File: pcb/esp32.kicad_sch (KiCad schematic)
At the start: 14 parts, among them J1 USB_C_Receptacle_USB2.0_16P, U1 ESP32-S3-WROOM-1, U2 AP2112K-3.3

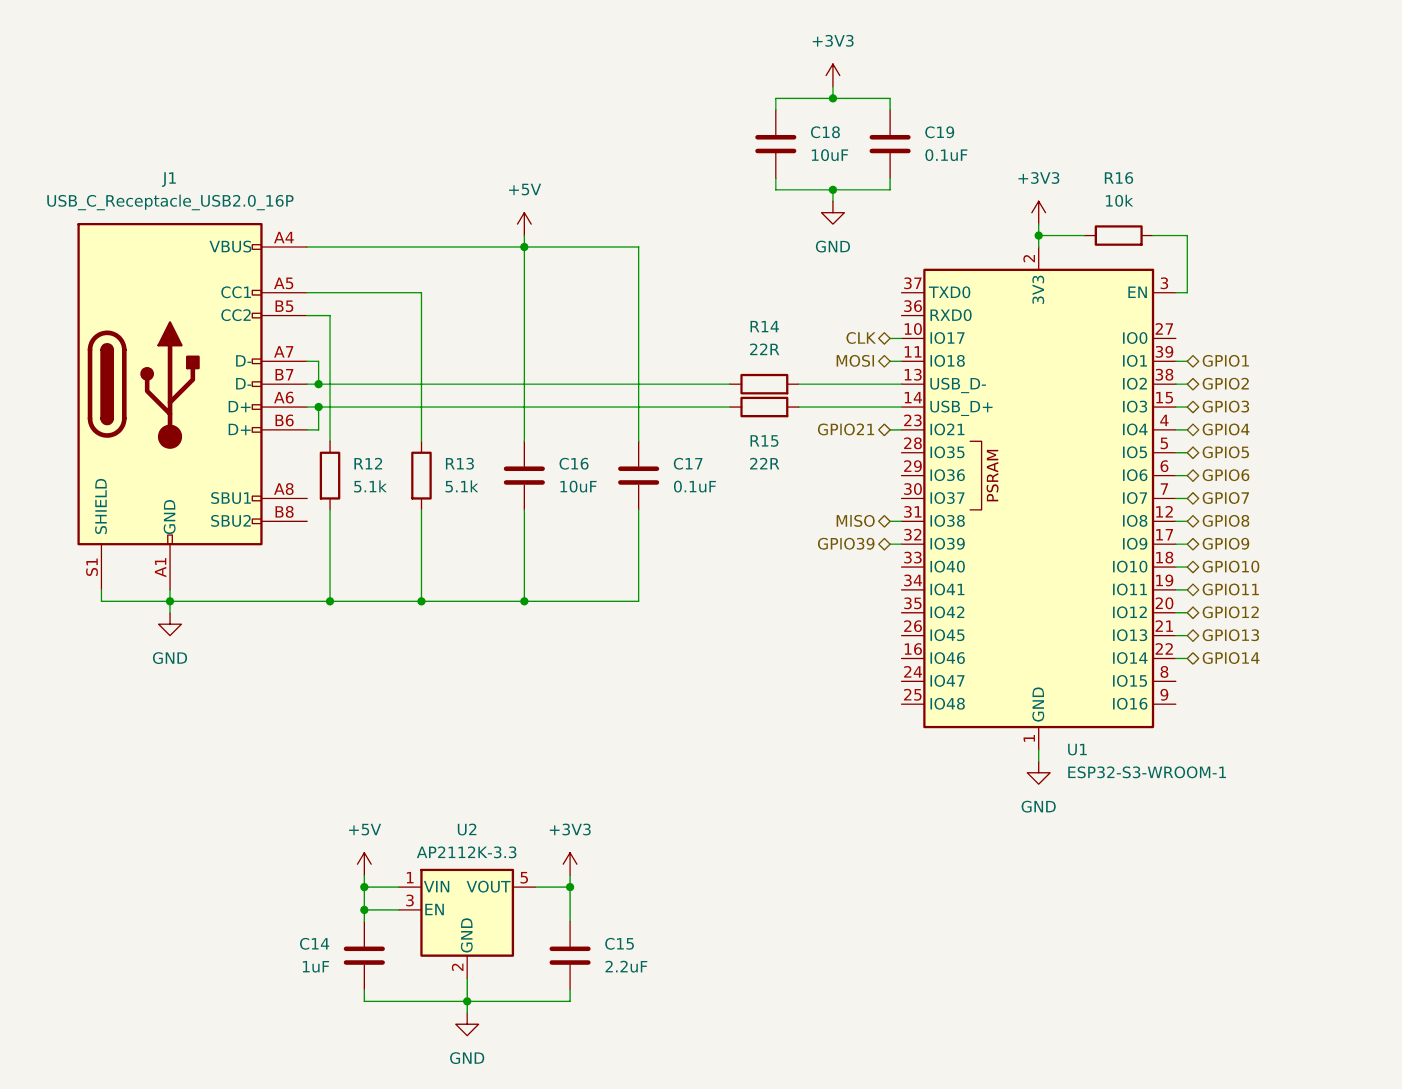
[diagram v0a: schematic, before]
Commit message: Fixed 3.3V connections and SD card orientation
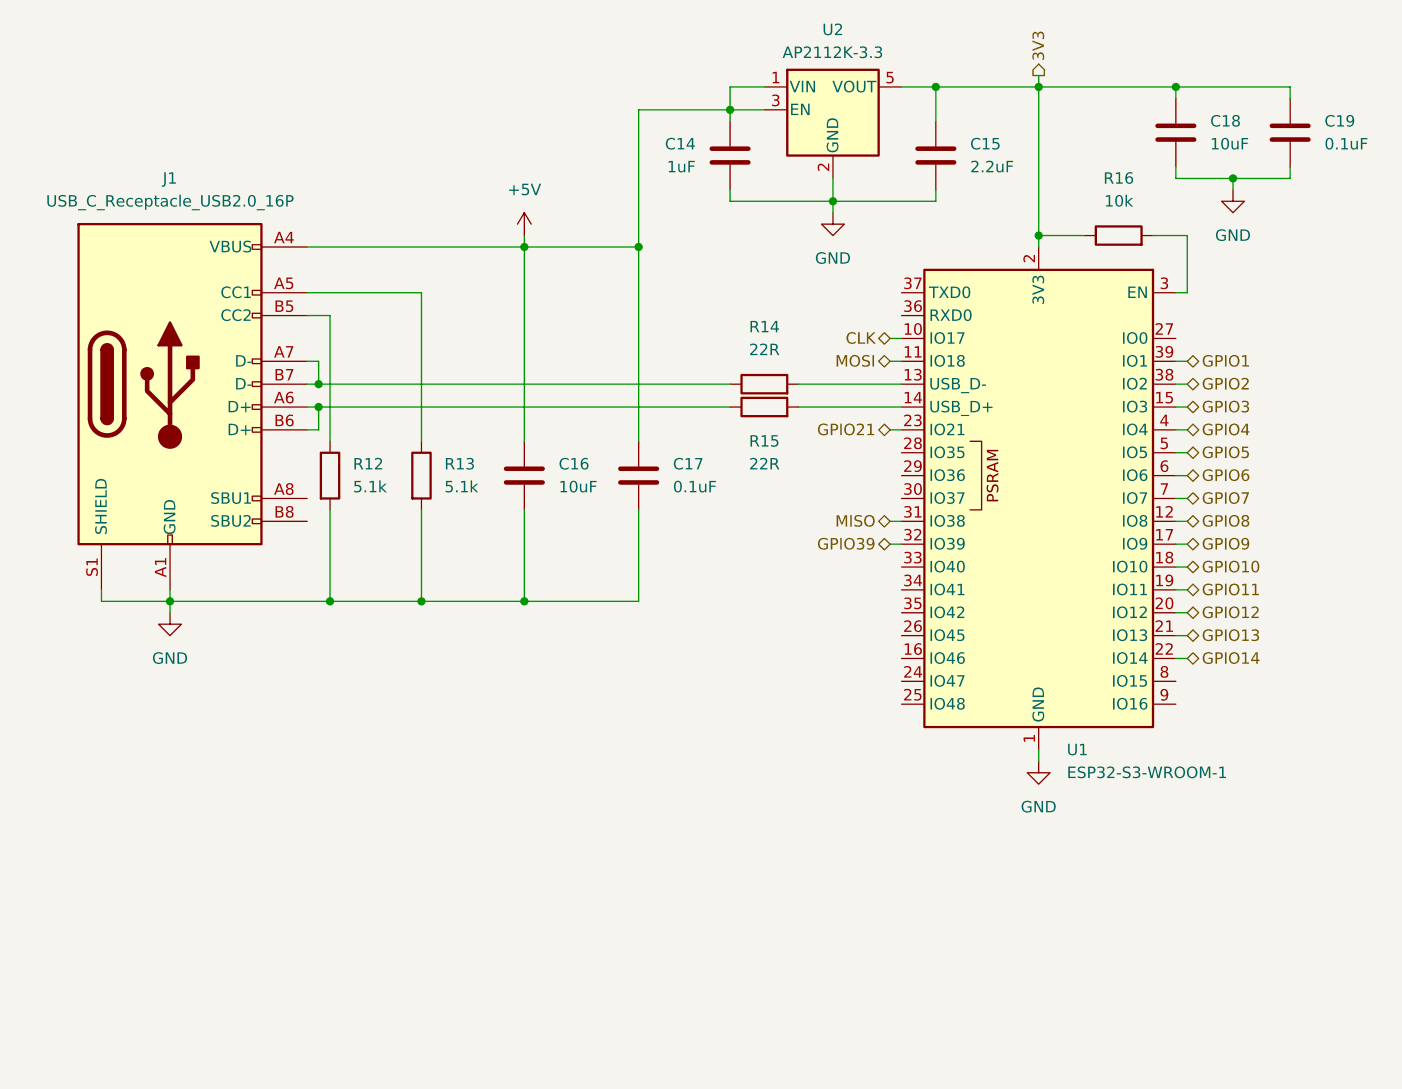
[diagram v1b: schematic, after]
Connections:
- net +3V3 renamed 3V3
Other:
- moved on the sheet: C14, C15, C18, C19, U2

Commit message: Added SSD1327 circuit
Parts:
- renumbered C16 to C1, C17 to C2, C14 to C3, C15 to C4, C18 to C5, C19 to C6, J1 to J2, U2 to U1, U1 to U2

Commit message: Split PCB into modules
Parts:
- renumbered C1 to C4, C2 to C5, C3 to C6, C4 to C7, C5 to C8, C6 to C9, J2 to J3, R12 to R4, R13 to R5, R14 to R6, R15 to R7, R16 to R8

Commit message: SSD1327 PCB routing
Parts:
- renumbered C4 to C3, C5 to C4, C6 to C5, C7 to C6, C8 to C7, C9 to C8, R4 to R3, R5 to R4, R6 to R5, R7 to R6, R8 to R7
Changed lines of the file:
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@@
 		(dnp no)
 		(fields_autoplaced yes)
-		(property "Reference" "R8"
+		(property "Reference" "R7"
 			(at 187.96 44.45 90)
 			(effects
@@
 		)
 		(instances
+			(project "ssd1327"
+				(path "/4342a6a3-bef3-4d00-bf81-0e0627ac4f3c/89317fe1-37c2-417c-ae91-da35df10ccc3"
+					(reference "R7")
+					(unit 1)
+				)
+			)
 			(project "ssd1322"
 				(path "/e965cf35-0f43-4e18-a922-fe79a625b049/6582fc17-a6be-4359-8e04-c0b6227802a5"
@@
 		(dnp no)
 		(fields_autoplaced yes)
-		(property "Reference" "R4"
+		(property "Reference" "R3"
 			(at 102.87 76.1999 0)
 			(effects
@@
 		)
 		(instances
+			(project "ssd1327"
+				(path "/4342a6a3-bef3-4d00-bf81-0e0627ac4f3c/89317fe1-37c2-417c-ae91-da35df10ccc3"
+					(reference "R3")
+					(unit 1)
+				)
+			)
 			(project "ssd1322"
 				(path "/e965cf35-0f43-4e18-a922-fe79a625b049/6582fc17-a6be-4359-8e04-c0b6227802a5"
@@
 		(dnp no)
 		(fields_autoplaced yes)
-		(property "Reference" "C4"
+		(property "Reference" "C3"
 			(at 125.73 76.1999 0)
 			(effects
@@
 		)
 		(instances
+			(project "ssd1327"
+				(path "/4342a6a3-bef3-4d00-bf81-0e0627ac4f3c/89317fe1-37c2-417c-ae91-da35df10ccc3"
+					(reference "C3")
+					(unit 1)
+				)
+			)
 			(project "ssd1322"
 				(path "/e965cf35-0f43-4e18-a922-fe79a625b049/6582fc17-a6be-4359-8e04-c0b6227802a5"
@@
 		)
 		(instances
+			(project "ssd1327"
+				(path "/4342a6a3-bef3-4d00-bf81-0e0627ac4f3c/89317fe1-37c2-417c-ae91-da35df10ccc3"
+					(reference "J3")
+					(unit 1)
+				)
+			)
 			(project "ssd1322"
 				(path "/e965cf35-0f43-4e18-a922-fe79a625b049/6582fc17-a6be-4359-8e04-c0b6227802a5"
@@
 		(dnp no)
 		(fields_autoplaced yes)
-		(property "Reference" "C8"
+		(property "Reference" "C7"
 			(at 198.12 38.0999 0)
 			(effects
@@
 		)
 		(instances
+			(project "ssd1327"
+				(path "/4342a6a3-bef3-4d00-bf81-0e0627ac4f3c/89317fe1-37c2-417c-ae91-da35df10ccc3"
+					(reference "C7")
+					(unit 1)
+				)
+			)
 			(project "ssd1322"
 				(path "/e965cf35-0f43-4e18-a922-fe79a625b049/6582fc17-a6be-4359-8e04-c0b6227802a5"
@@
 		)
 		(instances
+			(project "ssd1327"
+				(path "/4342a6a3-bef3-4d00-bf81-0e0627ac4f3c/89317fe1-37c2-417c-ae91-da35df10ccc3"
+					(reference "#PWR08")
+					(unit 1)
+				)
+			)
 			(project "ssd1322"
 				(path "/e965cf35-0f43-4e18-a922-fe79a625b049/6582fc17-a6be-4359-8e04-c0b6227802a5"
@@
 		(dnp no)
 		(fields_autoplaced yes)
-		(property "Reference" "R5"
+		(property "Reference" "R4"
 			(at 113.03 76.1999 0)
 			(effects
@@
 		)
 		(instances
+			(project "ssd1327"
+				(path "/4342a6a3-bef3-4d00-bf81-0e0627ac4f3c/89317fe1-37c2-417c-ae91-da35df10ccc3"
+					(reference "R4")
+					(unit 1)
+				)
+			)
 			(project "ssd1322"
 				(path "/e965cf35-0f43-4e18-a922-fe79a625b049/6582fc17-a6be-4359-8e04-c0b6227802a5"
@@
 		)
 		(instances
+			(project "ssd1327"
+				(path "/4342a6a3-bef3-4d00-bf81-0e0627ac4f3c/89317fe1-37c2-417c-ae91-da35df10ccc3"
+					(reference "#PWR06")
+					(unit 1)
+				)
+			)
 			(project "ssd1322"
 				(path "/e965cf35-0f43-4e18-a922-fe79a625b049/6582fc17-a6be-4359-8e04-c0b6227802a5"
@@
 		(dnp no)
 		(fields_autoplaced yes)
-		(property "Reference" "C5"
+		(property "Reference" "C4"
 			(at 138.43 76.1999 0)
 			(effects
@@
 		)
 		(instances
+			(project "ssd1327"
+				(path "/4342a6a3-bef3-4d00-bf81-0e0627ac4f3c/89317fe1-37c2-417c-ae91-da35df10ccc3"
+					(reference "C4")
+					(unit 1)
+				)
+			)
 			(project "ssd1322"
 				(path "/e965cf35-0f43-4e18-a922-fe79a625b049/6582fc17-a6be-4359-8e04-c0b6227802a5"
@@
 		)
 		(instances
+			(project "ssd1327"
+				(path "/4342a6a3-bef3-4d00-bf81-0e0627ac4f3c/89317fe1-37c2-417c-ae91-da35df10ccc3"
+					(reference "U1")
+					(unit 1)
+				)
+			)
 			(project "ssd1322"
 				(path "/e965cf35-0f43-4e18-a922-fe79a625b049/6582fc17-a6be-4359-8e04-c0b6227802a5"
@@
 		(dnp no)
 		(fields_autoplaced yes)
-		(property "Reference" "R7"
+		(property "Reference" "R6"
 			(at 148.59 73.66 90)
 			(effects
@@
 		)
 		(instances
+			(project "ssd1327"
+				(path "/4342a6a3-bef3-4d00-bf81-0e0627ac4f3c/89317fe1-37c2-417c-ae91-da35df10ccc3"
+					(reference "R6")
+					(unit 1)
+				)
+			)
 			(project "ssd1322"
 				(path "/e965cf35-0f43-4e18-a922-fe79a625b049/6582fc17-a6be-4359-8e04-c0b6227802a5"
@@
 		(dnp no)
 		(fields_autoplaced yes)
-		(property "Reference" "R6"
+		(property "Reference" "R5"
 			(at 148.59 60.96 90)
 			(effects
@@
 		)
 		(instances
+			(project "ssd1327"
+				(path "/4342a6a3-bef3-4d00-bf81-0e0627ac4f3c/89317fe1-37c2-417c-ae91-da35df10ccc3"
+					(reference "R5")
+					(unit 1)
+				)
+			)
 			(project "ssd1322"
 				(path "/e965cf35-0f43-4e18-a922-fe79a625b049/6582fc17-a6be-4359-8e04-c0b6227802a5"
@@
 		)
 		(instances
+			(project "ssd1327"
+				(path "/4342a6a3-bef3-4d00-bf81-0e0627ac4f3c/89317fe1-37c2-417c-ae91-da35df10ccc3"
+					(reference "#PWR05")
+					(unit 1)
+				)
+			)
 			(project "ssd1322"
 				(path "/e965cf35-0f43-4e18-a922-fe79a625b049/6582fc17-a6be-4359-8e04-c0b6227802a5"
@@
 		)
 		(instances
+			(project "ssd1327"
+				(path "/4342a6a3-bef3-4d00-bf81-0e0627ac4f3c/89317fe1-37c2-417c-ae91-da35df10ccc3"
+					(reference "U2")
+					(unit 1)
+				)
+			)
 			(project "ssd1322"
 				(path "/e965cf35-0f43-4e18-a922-fe79a625b049/6582fc17-a6be-4359-8e04-c0b6227802a5"
@@
 		(dnp no)
 		(fields_autoplaced yes)
-		(property "Reference" "C6"
+		(property "Reference" "C5"
 			(at 140.97 40.6399 0)
 			(effects
@@
 		)
 		(instances
+			(project "ssd1327"
+				(path "/4342a6a3-bef3-4d00-bf81-0e0627ac4f3c/89317fe1-37c2-417c-ae91-da35df10ccc3"
+					(reference "C5")
+					(unit 1)
+				)
+			)
 			(project "ssd1322"
 				(path "/e965cf35-0f43-4e18-a922-fe79a625b049/6582fc17-a6be-4359-8e04-c0b6227802a5"
@@
 		)
 		(instances
+			(project "ssd1327"
+				(path "/4342a6a3-bef3-4d00-bf81-0e0627ac4f3c/89317fe1-37c2-417c-ae91-da35df10ccc3"
+					(reference "#PWR07")
+					(unit 1)
+				)
+			)
 			(project "ssd1322"
 				(path "/e965cf35-0f43-4e18-a922-fe79a625b049/6582fc17-a6be-4359-8e04-c0b6227802a5"
@@
 		)
 		(instances
+			(project "ssd1327"
+				(path "/4342a6a3-bef3-4d00-bf81-0e0627ac4f3c/89317fe1-37c2-417c-ae91-da35df10ccc3"
+					(reference "#PWR04")
+					(unit 1)
+				)
+			)
 			(project "ssd1322"
 				(path "/e965cf35-0f43-4e18-a922-fe79a625b049/6582fc17-a6be-4359-8e04-c0b6227802a5"
@@
 		(dnp no)
 		(fields_autoplaced yes)
-		(property "Reference" "C9"
+		(property "Reference" "C8"
 			(at 210.82 38.0999 0)
 			(effects
@@
 		)
 		(instances
+			(project "ssd1327"
+				(path "/4342a6a3-bef3-4d00-bf81-0e0627ac4f3c/89317fe1-37c2-417c-ae91-da35df10ccc3"
+					(reference "C8")
+					(unit 1)
+				)
+			)
 			(project "ssd1322"
 				(path "/e965cf35-0f43-4e18-a922-fe79a625b049/6582fc17-a6be-4359-8e04-c0b6227802a5"
@@
 		(dnp no)
 		(fields_autoplaced yes)
-		(property "Reference" "C7"
+		(property "Reference" "C6"
 			(at 171.45 40.6399 0)
 			(effects
@@
 		)
 		(instances
-			(project "ssd1322"
-				(path "/e965cf35-0f43-4e18-a922-fe79a625b049/6582fc17-a6be-4359-8e04-c0b6227802a5"
+			(project "ssd1327"
+				(path "/4342a6a3-bef3-4d00-bf81-0e0627ac4f3c/89317fe1-37c2-417c-ae91-da35df10ccc3"
+					(reference "C6")
+					(unit 1)
+				)
+			)
+			(project "ssd1322"
+				(path "/e965cf35-0f43-4e18-a922-fe79a625b049/6582fc17-a6be-4359-8e04-c0b6227802a5"

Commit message: Master board PCB routing
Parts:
- renumbered C3 to C1, C4 to C2, C5 to C3, C6 to C4, C7 to C5, C8 to C6, J3 to J5, R4 to R10, R5 to R11, R6 to R12, R7 to R13, R3 to R9
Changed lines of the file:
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@@
 		(dnp no)
 		(fields_autoplaced yes)
-		(property "Reference" "R7"
+		(property "Reference" "R13"
 			(at 187.96 44.45 90)
 			(effects
@@
 		(dnp no)
 		(fields_autoplaced yes)
-		(property "Reference" "R3"
+		(property "Reference" "R9"
 			(at 102.87 76.1999 0)
 			(effects
@@
 		(dnp no)
 		(fields_autoplaced yes)
-		(property "Reference" "C3"
+		(property "Reference" "C1"
 			(at 125.73 76.1999 0)
 			(effects
@@
 		(dnp no)
 		(fields_autoplaced yes)
-		(property "Reference" "J3"
+		(property "Reference" "J5"
 			(at 82.55 44.45 0)
 			(effects
@@
 		(dnp no)
 		(fields_autoplaced yes)
-		(property "Reference" "C7"
+		(property "Reference" "C5"
 			(at 198.12 38.0999 0)
 			(effects
@@
 		(dnp no)
 		(fields_autoplaced yes)
-		(property "Reference" "#PWR08"
+		(property "Reference" "#PWR014"
 			(at 200.66 52.07 0)
 			(effects
@@
 		(dnp no)
 		(fields_autoplaced yes)
-		(property "Reference" "R4"
+		(property "Reference" "R10"
 			(at 113.03 76.1999 0)
 			(effects
@@
 		(dnp no)
 		(fields_autoplaced yes)
-		(property "Reference" "#PWR06"
+		(property "Reference" "#PWR012"
 			(at 156.21 54.61 0)
 			(effects
@@
 		(dnp no)
 		(fields_autoplaced yes)
-		(property "Reference" "C4"
+		(property "Reference" "C2"
 			(at 138.43 76.1999 0)
 			(effects
@@
 		(dnp no)
 		(fields_autoplaced yes)
-		(property "Reference" "R6"
+		(property "Reference" "R12"
 			(at 148.59 73.66 90)
 			(effects
@@
 		(dnp no)
 		(fields_autoplaced yes)
-		(property "Reference" "R5"
+		(property "Reference" "R11"
 			(at 148.59 60.96 90)
 			(effects
@@
 		(dnp no)
 		(fields_autoplaced yes)
-		(property "Reference" "#PWR05"
+		(property "Reference" "#PWR011"
 			(at 121.92 54.61 0)
 			(effects
@@
 		(dnp no)
 		(fields_autoplaced yes)
-		(property "Reference" "C5"
+		(property "Reference" "C3"
 			(at 140.97 40.6399 0)
 			(effects
@@
 		(dnp no)
 		(fields_autoplaced yes)
-		(property "Reference" "#PWR07"
+		(property "Reference" "#PWR013"
 			(at 179.07 115.57 0)
 			(effects
@@
 		(dnp no)
 		(fields_autoplaced yes)
-		(property "Reference" "#PWR04"
+		(property "Reference" "#PWR010"
 			(at 82.55 99.06 0)
 			(effects
@@
 		(dnp no)
 		(fields_autoplaced yes)
-		(property "Reference" "C8"
+		(property "Reference" "C6"
 			(at 210.82 38.0999 0)
 			(effects
@@
 		(dnp no)
 		(fields_autoplaced yes)
-		(property "Reference" "C6"
+		(property "Reference" "C4"
 			(at 171.45 40.6399 0)
 			(effects
